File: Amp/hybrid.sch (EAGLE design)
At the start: 123 parts, among them IC1 TL071P, IC2 TL071P, IC3 LM317MABT, IC4 LM317MABT, J2 NRJ3HF-1, Q1 KSP06KINKED, Q10 BD139, Q11 KSP06KINKED, Q12 BC560KINKED, Q13 BC560KINKED, Q14 BC560KINKED, Q15 BC556KINKED, Q16 BC550KINKED, Q17 BC550KINKED, Q18 BC560KINKED, Q19 BD140, Q2 BC560KINKED, Q20 BD139, Q21 KSP43, Q22 KSP43, Q3 BC560KINKED, Q4 BC560KINKED, Q5 BC556KINKED, Q6 BC550KINKED, Q7 BC550KINKED, Q8 BC560KINKED, Q9 BD140

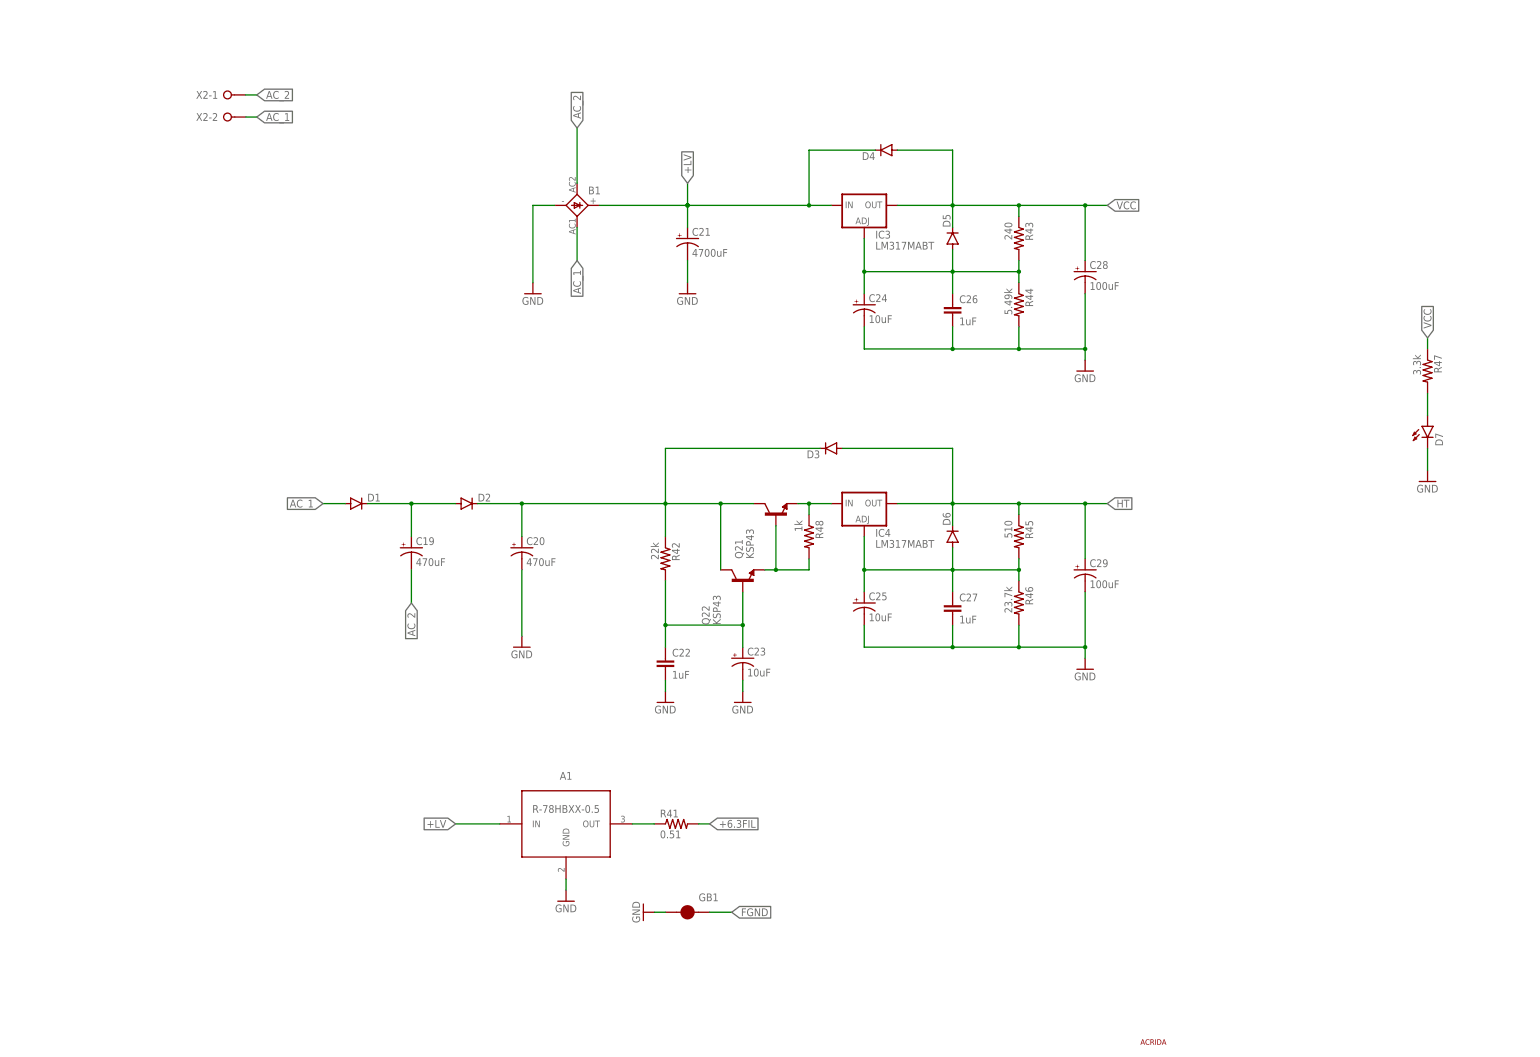
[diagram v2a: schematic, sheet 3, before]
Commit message: Optional protection circuit
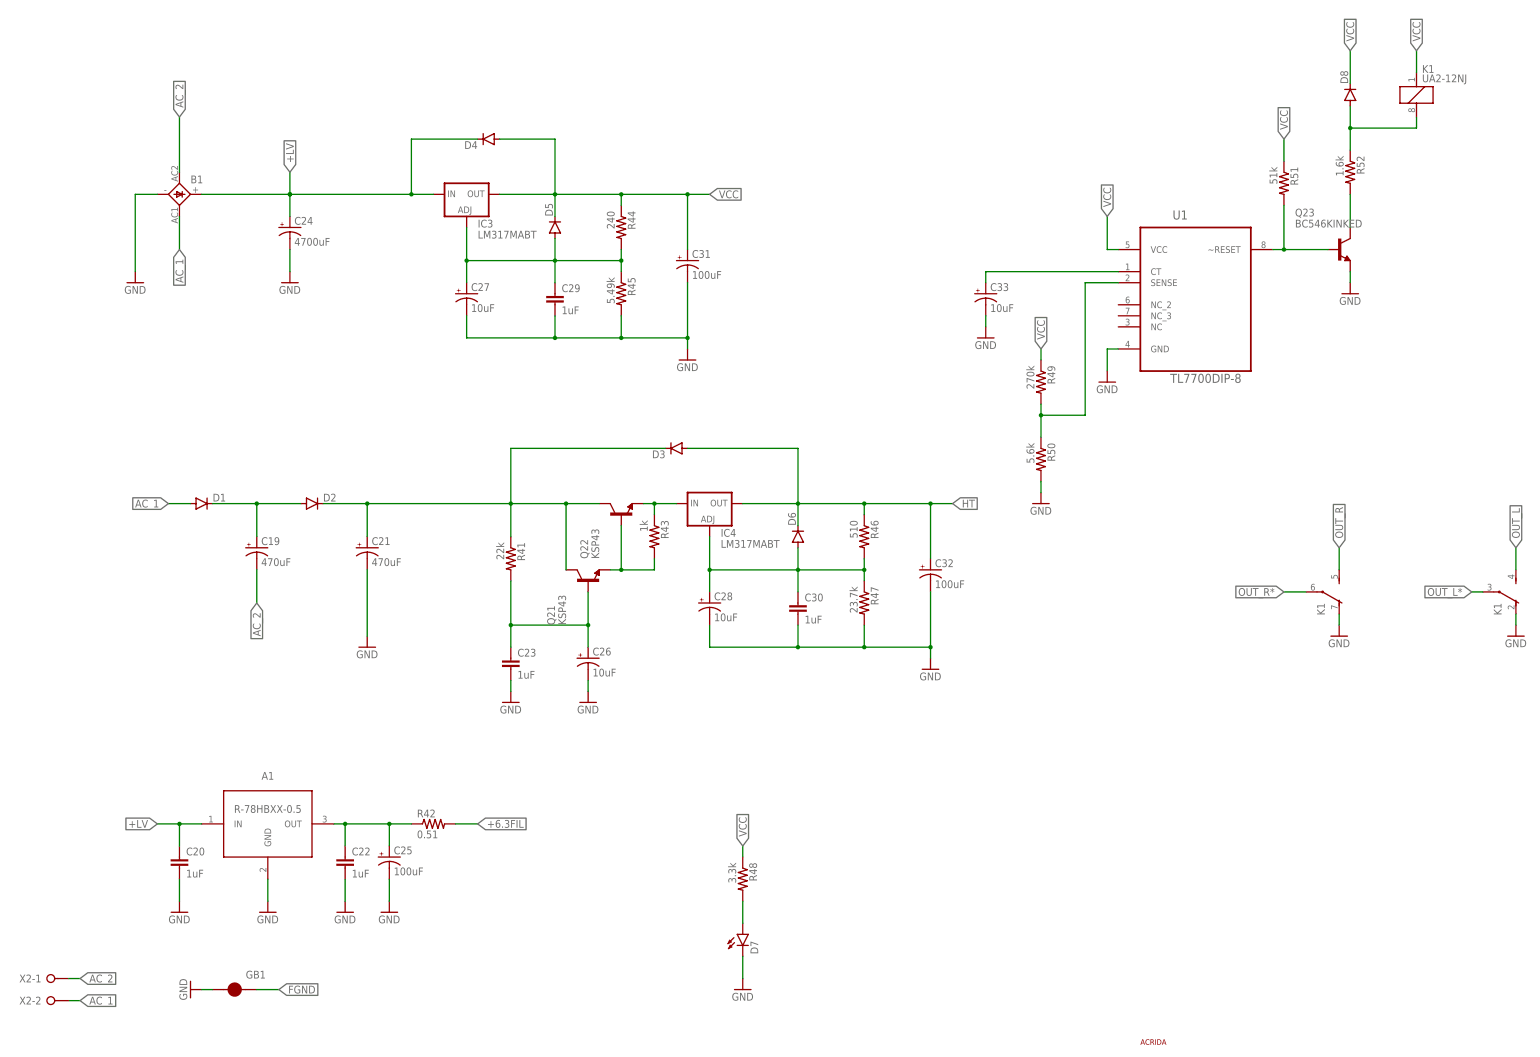
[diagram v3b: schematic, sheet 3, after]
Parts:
- added C30: 1uF, SparkFun-Capacitors:CAPPTH
- added C31, C32: 100uF, my-cap:CAP_POLPTH-12.5/5
- added C33: 10uF, my-cap:CAP_POLPTH-5/2.5
- added D8: (no value), SparkFun-DiscreteSemi:DIODEKIT
- added K1: UA2-12NJ, my-relay:UA2-12NJ
- added Q23: BC546KINKED, my-tran:BC546KINKED
- added R49: 270k, SparkFun-Resistors:RESISTORPTH-1/4W
- added R50: 5.6k, SparkFun-Resistors:RESISTORPTH-1/4W
- added R51: 51k, SparkFun-Resistors:RESISTORPTH-1/4W
- added R52: 1.6k, SparkFun-Resistors:RESISTORPTH-1/4W
- added U1: TL7700DIP-8, my-ic:TL7700DIP-8
- C20: value 470uF -> 1uF; device my-cap:CAP_POLPTH-18/7.5 -> SparkFun-Capacitors:CAPPTH1
- C21: value 4700uF -> 470uF; device my-cap:CAP_POLSNAPIN-30/10 -> my-cap:CAP_POLPTH-18/7.5
- C22: device SparkFun-Capacitors:CAPPTH1 -> SparkFun-Capacitors:CAPPTH
- C23: value 10uF -> 1uF; device my-cap:CAP_POLPTH-12/5 -> SparkFun-Capacitors:CAPPTH1
- C24: value 10uF -> 4700uF; device my-cap:CAP_POLPTH-5/2.5 -> my-cap:CAP_POLSNAPIN-30/10
- C25: value 10uF -> 100uF
- C26: value 1uF -> 10uF; device SparkFun-Capacitors:CAPPTH -> my-cap:CAP_POLPTH-12/5
- C27: value 1uF -> 10uF; device SparkFun-Capacitors:CAPPTH -> my-cap:CAP_POLPTH-5/2.5
- C28: value 100uF -> 10uF; device my-cap:CAP_POLPTH-12.5/5 -> my-cap:CAP_POLPTH-6.5/2.5
- C29: value 100uF -> 1uF; device my-cap:CAP_POLPTH-12.5/5 -> SparkFun-Capacitors:CAPPTH
- R41: value 0.51 -> 22k; device my-res:RESISTORPTH-1/2W -> SparkFun-Resistors:RESISTORPTH-1/4W
- R42: value 22k -> 0.51; device SparkFun-Resistors:RESISTORPTH-1/4W -> my-res:RESISTORPTH-1/2W
- R43: value 240 -> 1k
- R44: value 5.49k -> 240
- R45: value 510 -> 5.49k
- R46: value 23.7k -> 510
- R47: value 3.3k -> 23.7k
- R48: value 1k -> 3.3k
- renumbered J2 to J1
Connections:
- new net N$40: C33.+, U1.CT
- new net N$44: Q23.B, R51.2, U1.~RESET
- new net N$45: R49.2, R50.1, U1.SENSE
- new net N$49: D8.A, K11.2, R52.1
- new net N$50: Q23.C, R52.2
- new net OUT_L*: J1.LEFT, K12.P
- new net OUT_R*: J1.RIGHT, K13.P
- net +6.3FIL: now also R42.2; no longer R41.2
- net +LV: now also C20.1, C24.+; no longer C21.+
- net GND: now also C20.2, C23.2, C26.-, C27.-, C29.2, C30.2, C31.-, C32.-, C33.-, K12.O, K13.O, Q23.E, R45.2, R47.2, R50.2, U1.GND; no longer C20.-, C23.-, C26.2, C27.2, C29.-, R44.2, R46.2
- net HT: now also C32.+, R46.1; no longer C29.+, R45.1
- net N$18: now also Q21.E, Q22.B, R43.2; no longer Q21.B, Q22.E, R48.2
- net N$30: now also C27.+, C29.1, R44.2, R45.1; no longer C24.+, C26.1, R43.2, R44.1
- net N$32: now also C22.1, C25.+, R42.1; no longer R41.1
- net N$33: now also C21.+, R41.1; no longer C20.+, R42.1
- net N$34: now also C23.1, C26.+, Q21.B, R41.2; no longer C22.1, C23.+, Q22.B, R42.2
- net N$36: now also C28.+, C30.1, R46.2, R47.1; no longer C25.+, C27.1, R45.2, R46.1
- net N$37: now also Q22.E, R43.1; no longer Q21.E, R48.1
- net N$46: now also R48.2; no longer R47.2
- net OUT_L: now also K12.S; no longer J1.LEFT
- net OUT_R: now also K13.S; no longer J1.RIGHT
- net VCC: now also C31.+, D8.C, K11.1, R44.1, R48.1, R49.1, R51.1, U1.VCC; no longer C28.+, R43.1, R47.1
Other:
- moved on the sheet: A1, B1, C19, C21, C22, C24, C25, C28, D1, D2, D3, D4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

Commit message: Final polishing
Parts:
- C27, C33: device my-cap:CAP_POLPTH-5/2.5 -> my-cap:CAP_POLPTH-6.5/2.5
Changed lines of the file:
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@@
 <grid distance="0.1" unitdist="inch" unit="inch" style="lines" multiple="1" display="no" altdistance="0.01" altunitdist="inch" altunit="inch"/>
 <layers>
-<layer number="1" name="Top" color="4" fill="1" visible="no" active="no"/>
-<layer number="2" name="Route2" color="1" fill="3" visible="no" active="no"/>
-<layer number="3" name="Route3" color="4" fill="3" visible="no" active="no"/>
-<layer number="4" name="Route4" color="1" fill="4" visible="no" active="no"/>
-<layer number="5" name="Route5" color="4" fill="4" visible="no" active="no"/>
-<layer number="6" name="Route6" color="1" fill="8" visible="no" active="no"/>
-<layer number="7" name="Route7" color="4" fill="8" visible="no" active="no"/>
-<layer number="8" name="Route8" color="1" fill="2" visible="no" active="no"/>
-<layer number="9" name="Route9" color="4" fill="2" visible="no" active="no"/>
-<layer number="10" name="Route10" color="1" fill="7" visible="no" active="no"/>
-<layer number="11" name="Route11" color="4" fill="7" visible="no" active="no"/>
-<layer number="12" name="Route12" color="1" fill="5" visible="no" active="no"/>
-<layer number="13" name="Route13" color="4" fill="5" visible="no" active="no"/>
-<layer number="14" name="Route14" color="1" fill="6" visible="no" active="no"/>
-<layer number="15" name="Route15" color="4" fill="6" visible="no" active="no"/>
-<layer number="16" name="Bottom" color="1" fill="1" visible="no" active="no"/>
-<layer number="17" name="Pads" color="2" fill="1" visible="no" active="no"/>
-<layer number="18" name="Vias" color="2" fill="1" visible="no" active="no"/>
-<layer number="19" name="Unrouted" color="6" fill="1" visible="no" active="no"/>
-<layer number="20" name="Dimension" color="15" fill="1" visible="no" active="no"/>
-<layer number="21" name="tPlace" color="7" fill="1" visible="no" active="no"/>
-<layer number="22" name="bPlace" color="7" fill="1" visible="no" active="no"/>
-<layer number="23" name="tOrigins" color="15" fill="1" visible="no" active="no"/>
-<layer number="24" name="bOrigins" color="15" fill="1" visible="no" active="no"/>
-<layer number="25" name="tNames" color="7" fill="1" visible="no" active="no"/>
-<layer number="26" name="bNames" color="7" fill="1" visible="no" active="no"/>
-<layer number="27" name="tValues" color="7" fill="1" visible="no" active="no"/>
-<layer number="28" name="bValues" color="7" fill="1" visible="no" active="no"/>
+<layer number="1" name="Top" color="4" fill="1" visible="yes" active="no"/>
+<layer number="2" name="Route2" color="1" fill="3" visible="yes" active="no"/>
+<layer number="3" name="Route3" color="4" fill="3" visible="yes" active="no"/>
+<layer number="4" name="Route4" color="1" fill="4" visible="yes" active="no"/>
+<layer number="5" name="Route5" color="4" fill="4" visible="yes" active="no"/>
+<layer number="6" name="Route6" color="1" fill="8" visible="yes" active="no"/>
+<layer number="7" name="Route7" color="4" fill="8" visible="yes" active="no"/>
+<layer number="8" name="Route8" color="1" fill="2" visible="yes" active="no"/>
+<layer number="9" name="Route9" color="4" fill="2" visible="yes" active="no"/>
+<layer number="10" name="Route10" color="1" fill="7" visible="yes" active="no"/>
+<layer number="11" name="Route11" color="4" fill="7" visible="yes" active="no"/>
+<layer number="12" name="Route12" color="1" fill="5" visible="yes" active="no"/>
+<layer number="13" name="Route13" color="4" fill="5" visible="yes" active="no"/>
+<layer number="14" name="Route14" color="1" fill="6" visible="yes" active="no"/>
+<layer number="15" name="Route15" color="4" fill="6" visible="yes" active="no"/>
+<layer number="16" name="Bottom" color="1" fill="1" visible="yes" active="no"/>
+<layer number="17" name="Pads" color="2" fill="1" visible="yes" active="no"/>
+<layer number="18" name="Vias" color="2" fill="1" visible="yes" active="no"/>
+<layer number="19" name="Unrouted" color="6" fill="1" visible="yes" active="no"/>
+<layer number="20" name="Dimension" color="15" fill="1" visible="yes" active="no"/>
+<layer number="21" name="tPlace" color="7" fill="1" visible="yes" active="no"/>
+<layer number="22" name="bPlace" color="7" fill="1" visible="yes" active="no"/>
+<layer number="23" name="tOrigins" color="15" fill="1" visible="yes" active="no"/>
+<layer number="24" name="bOrigins" color="15" fill="1" visible="yes" active="no"/>
+<layer number="25" name="tNames" color="7" fill="1" visible="yes" active="no"/>
+<layer number="26" name="bNames" color="7" fill="1" visible="yes" active="no"/>
+<layer number="27" name="tValues" color="7" fill="1" visible="yes" active="no"/>
+<layer number="28" name="bValues" color="7" fill="1" visible="yes" active="no"/>
 <layer number="29" name="tStop" color="7" fill="3" visible="no" active="no"/>
 <layer number="30" name="bStop" color="7" fill="6" visible="no" active="no"/>
@@
 <layer number="35" name="tGlue" color="7" fill="4" visible="no" active="no"/>
 <layer number="36" name="bGlue" color="7" fill="5" visible="no" active="no"/>
-<layer number="37" name="tTest" color="7" fill="1" visible="no" active="no"/>
-<layer number="38" name="bTest" color="7" fill="1" visible="no" active="no"/>
+<layer number="37" name="tTest" color="7" fill="1" visible="yes" active="no"/>
+<layer number="38" name="bTest" color="7" fill="1" visible="yes" active="no"/>
 <layer number="39" name="tKeepout" color="4" fill="11" visible="no" active="no"/>
 <layer number="40" name="bKeepout" color="1" fill="11" visible="no" active="no"/>
@@
 <layer number="44" name="Drills" color="7" fill="1" visible="no" active="no"/>
 <layer number="45" name="Holes" color="7" fill="1" visible="no" active="no"/>
-<layer number="46" name="Milling" color="3" fill="1" visible="no" active="no"/>
-<layer number="47" name="Measures" color="7" fill="1" visible="no" active="no"/>
-<layer number="48" name="Document" color="7" fill="1" visible="no" active="no"/>
-<layer number="49" name="Reference" color="7" fill="1" visible="no" active="no"/>
-<layer number="50" name="dxf" color="7" fill="1" visible="no" active="no"/>
-<layer number="51" name="tDocu" color="7" fill="1" visible="no" active="no"/>
-<layer number="52" name="bDocu" color="7" fill="1" visible="no" active="no"/>
-<layer number="53" name="tGND_GNDA" color="7" fill="9" visible="no" active="no"/>
-<layer number="54" name="bGND_GNDA" color="1" fill="9" visible="no" active="no"/>
-<layer number="56" name="wert" color="7" fill="1" visible="no" active="no"/>
-<layer number="57" name="tCAD" color="7" fill="1" visible="no" active="no"/>
-<layer number="59" name="tCarbon" color="7" fill="1" visible="no" active="no"/>
-<layer number="60" name="bCarbon" color="7" fill="1" visible="no" active="no"/>
+<layer number="46" name="Milling" color="3" fill="1" visible="yes" active="no"/>
+<layer number="47" name="Measures" color="7" fill="1" visible="yes" active="no"/>
+<layer number="48" name="Document" color="7" fill="1" visible="yes" active="no"/>
+<layer number="49" name="Reference" color="7" fill="1" visible="yes" active="no"/>
+<layer number="50" name="dxf" color="7" fill="1" visible="yes" active="no"/>
+<layer number="51" name="tDocu" color="7" fill="1" visible="yes" active="no"/>
+<layer number="52" name="bDocu" color="7" fill="1" visible="yes" active="no"/>
+<layer number="53" name="tGND_GNDA" color="7" fill="9" visible="yes" active="no"/>
+<layer number="54" name="bGND_GNDA" color="1" fill="9" visible="yes" active="no"/>
+<layer number="56" name="wert" color="7" fill="1" visible="yes" active="no"/>
+<layer number="57" name="tCAD" color="7" fill="1" visible="yes" active="no"/>
+<layer number="59" name="tCarbon" color="7" fill="1" visible="yes" active="no"/>
+<layer number="60" name="bCarbon" color="7" fill="1" visible="yes" active="no"/>
 <layer number="90" name="Modules" color="5" fill="1" visible="yes" active="yes"/>
 <layer number="91" name="Nets" color="2" fill="1" visible="yes" active="yes"/>
@@
 <part name="GND40" library="SparkFun-Aesthetics" deviceset="GND" device=""/>
 <part name="C29" library="SparkFun-Capacitors" deviceset="CAP" device="PTH" value="1uF"/>
-<part name="C27" library="my-cap" deviceset="CAP_POL" device="PTH-5/2.5" value="10uF"/>
+<part name="C27" library="my-cap" deviceset="CAP_POL" device="PTH-6.5/2.5" value="10uF"/>
 <part name="D5" library="SparkFun-DiscreteSemi" deviceset="DIODE" device="PTH"/>
 <part name="D4" library="SparkFun-DiscreteSemi" deviceset="DIODE" device="PTH"/>
@@
 <part name="GND38" library="SparkFun-Aesthetics" deviceset="GND" device=""/>
 <part name="U1" library="my-ic" deviceset="TL7700" device="DIP-8"/>
-<part name="C33" library="my-cap" deviceset="CAP_POL" device="PTH-5/2.5" value="10uF"/>
+<part name="C33" library="my-cap" deviceset="CAP_POL" device="PTH-6.5/2.5" value="10uF"/>
 <part name="GND43" library="SparkFun-Aesthetics" deviceset="GND" device=""/>
 <part name="GND44" library="SparkFun-Aesthetics" deviceset="GND" device=""/>
